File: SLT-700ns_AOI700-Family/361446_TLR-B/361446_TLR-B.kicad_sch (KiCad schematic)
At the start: 9 parts, among them T1 CB, T2 CC, T3 AAD, U1 12-Pin_SLx_Can

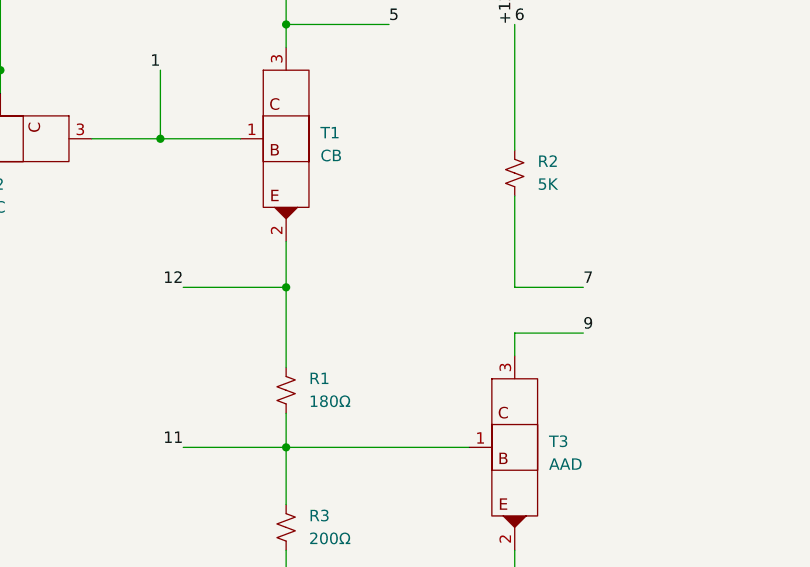
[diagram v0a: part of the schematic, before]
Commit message: Add can P/N to schematics for SLT-700
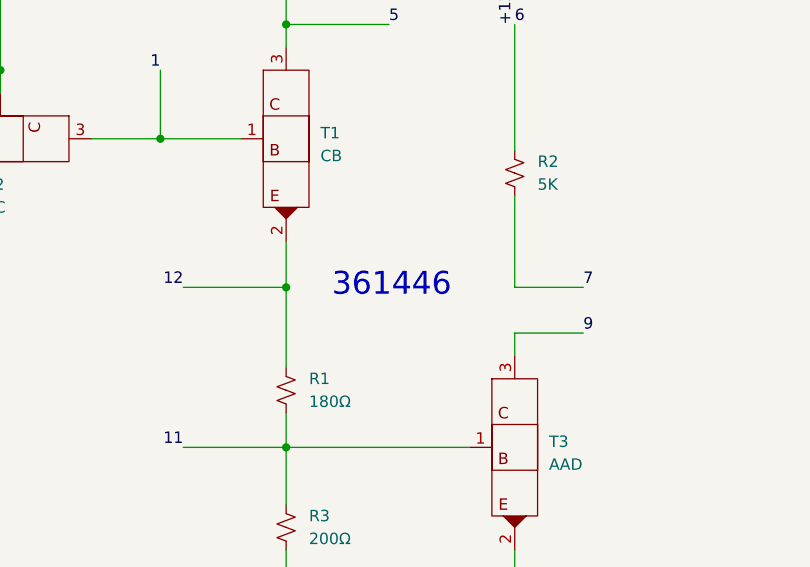
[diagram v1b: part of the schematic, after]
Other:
- note added: "361446"
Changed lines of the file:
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@@
     (stroke (width 0) (type default) (color 0 0 0 0))
+  )
+  (text "361446" (at 137.16 100.33 0)
+    (effects (font (size 2.54 2.54)) (justify left bottom))
   )
   (text "R.C. Module" (at 110.49 46.99 0)
